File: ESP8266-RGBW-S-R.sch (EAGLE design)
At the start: 57 parts, among them IC1 ATTINY85, IC2 ESP8266-ESP12, IC6 LM1117-3.3, K1 SONGLE-RELAY-SPDT, K2 OMRON-G3MB-OPTO-RELAY, Q1 BC317, Q2 BC317, Q3 SO340020, Q4 SO340020, Q5 SO340020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

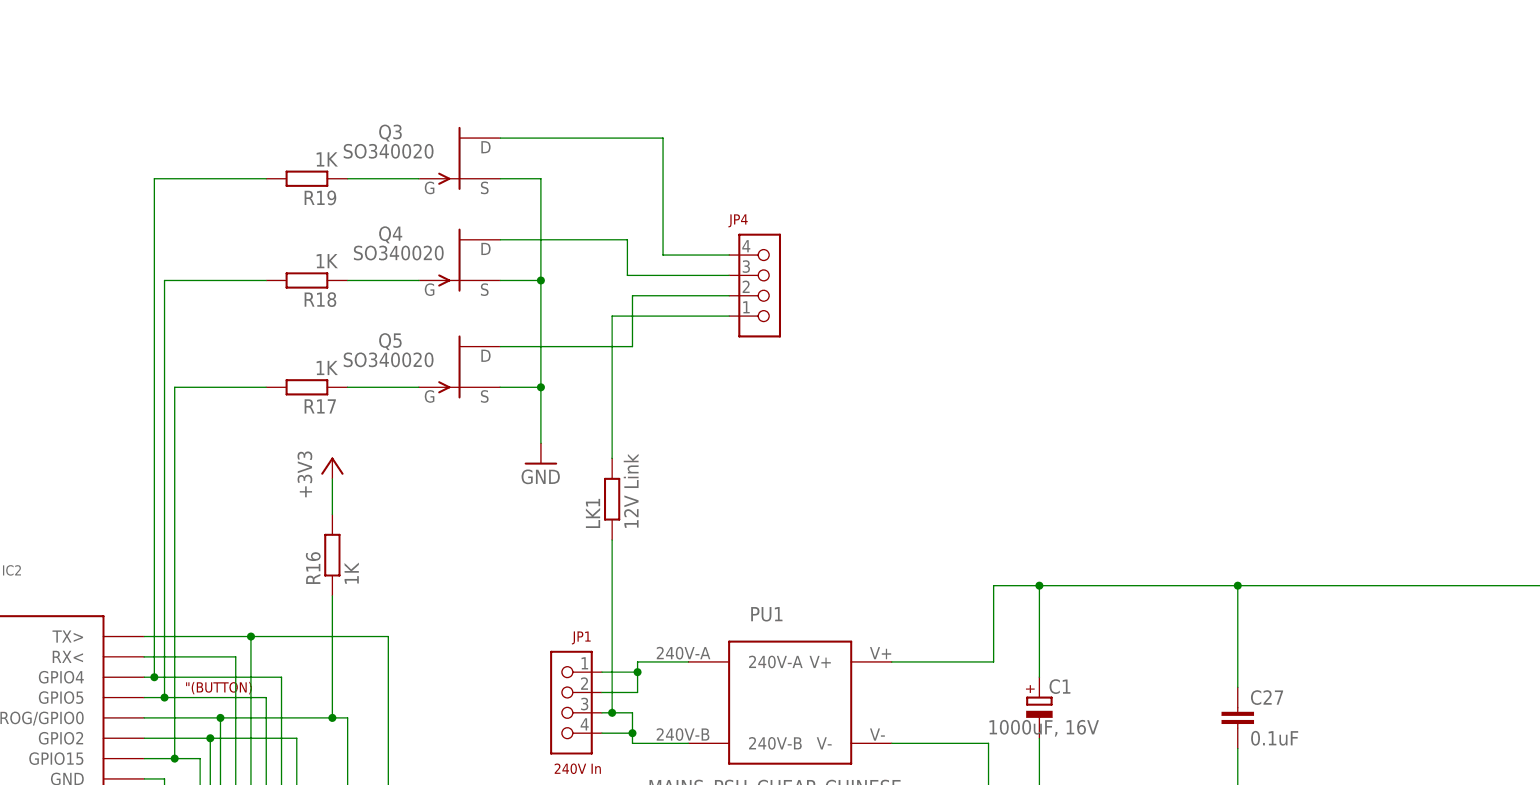
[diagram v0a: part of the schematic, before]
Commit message: added White channel for PWM output
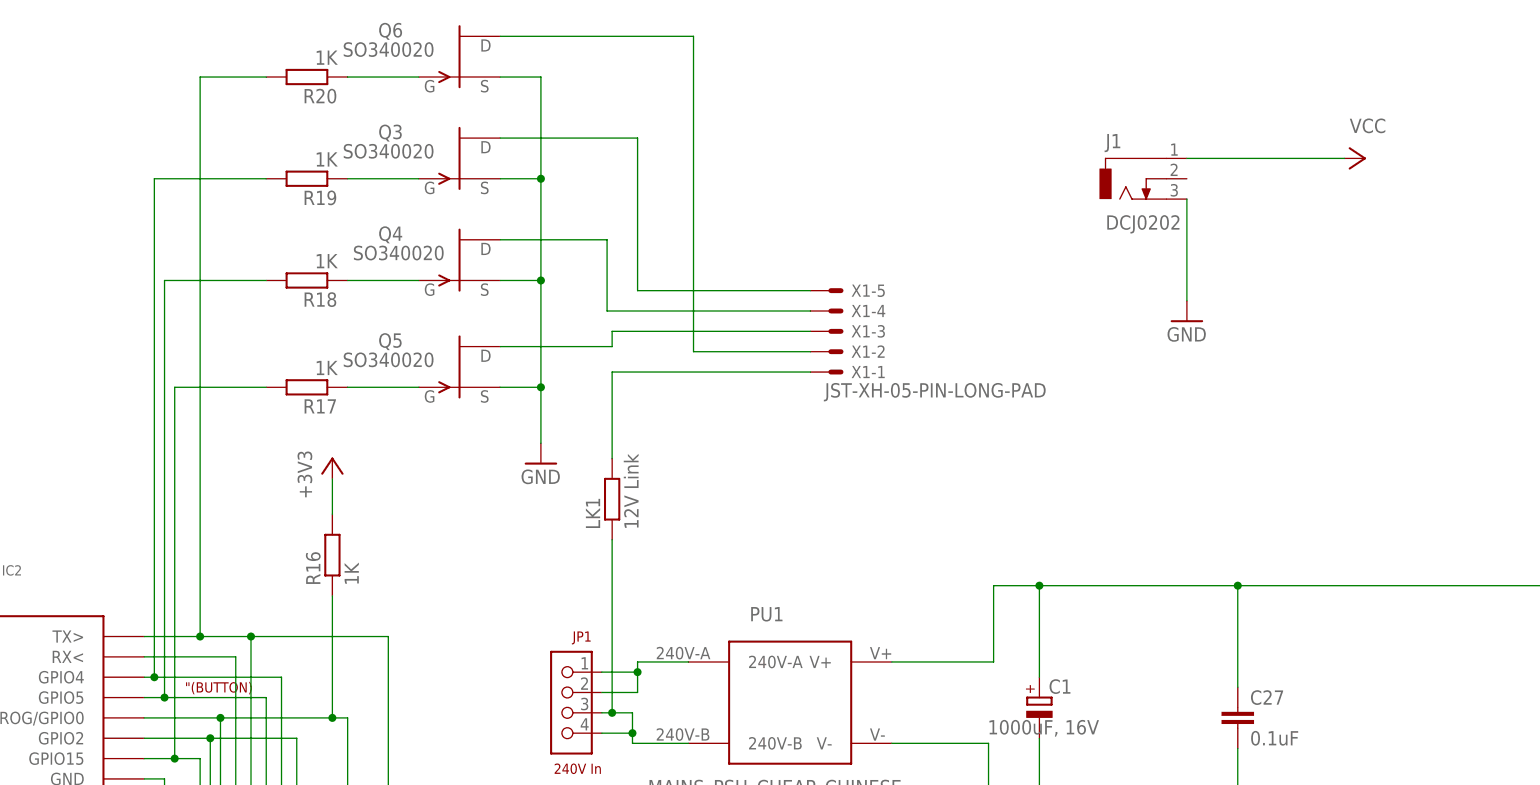
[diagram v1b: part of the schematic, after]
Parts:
- removed JP4: HDR4X0.1, Aidans:HDR4X0.1
- added J1: DCJ0202, con-jack:DCJ0202
- added Q6: SO340020, transistor-fet:SO340020
- added R20: 1K, resistor:R-EU_R0805
- added X1: JST-XH-05-PIN-LONG-PAD, Rembrandt Electronics - JST XH Connectors v1-0:JST-XH-05-PIN-LONG-PAD
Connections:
- removed net N$152: IC2.TX>, JP10.P$5, WIFI2.1
- new net GPIO3: IC2.TX>, JP10.P$5, R20.2, WIFI2.1
- new net N$117: Q3.D, X1-5.S
- new net N$118: Q6.G, R20.1
- net GND: now also J1.3, Q6.S
- net N$12: now also Q6.D, X1-2.S; no longer JP4.P$4, Q3.D
- net N$14: now also Q5.D, X1-3.S; no longer JP4.P$3, Q4.D
- net N$79: now also Q4.D, X1-4.S; no longer JP4.P$2, Q5.D
- net N$80: now also X1-1.S; no longer JP4.P$1
- net VCC: now also J1.1

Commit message: alternative power subbly (DC-DC, AC-DC), alternative power jack as input
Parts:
- removed PU1: MAINS_PSU_CHEAP_CHINESE, Aidans:MAINS_PSU_CHEAP_CHINESE
- added J3: WJ300-5.0, SparkFun-Connectors-2pin:CONN_02PTH4
- added JP4: V+V, pinhead:PINHD-1X2
- added PSU-A: HLK-PM013W, 5:HLK-PM013W
- added PSU-B: B0503S, dc-dc-converter:NME
- added PSU-C: DC-DC-STEP-DOWN-LM2596, diy-modules:DC-DC-STEP-DOWN-LM2596
- added PSU-D: HLK-2M03, HLK-2M03:HLK-2M03
- J1: value DCJ0202 -> POWER_JACKPTH_LOCK; device con-jack:DCJ0202 -> SparkFun-Connectors:POWER_JACKPTH_LOCK
- JP1: value 240V In -> GND+GND; device Aidans:4X0.2 -> pinhead:PINHD-1X2
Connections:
- removed net N$3: JP1.P$1, JP1.P$2, PU1.240V-A
- removed net N$5: JP1.P$3, JP1.P$4, LK1.1, PU1.240V-B
- new net +VCC: C1.+, C2.1, C27.1, C3.1, D1.C, IC6.IN, JP10.P$3, JP4.1, JP7.P$7, JP7.P$8, K1.C1, PSU-A.+VO
- new net V+: J1.PWR, J3.1, LK1.1, PSU-A.AC1, PSU-B.+VIN, PSU-C.IN+, PSU-D.AC_1
- new net V-: J1.GND, J3.2, PSU-A.AC2, PSU-B.-VIN, PSU-C.IN-, PSU-D.AC_2
- net +3V3: now also JP4.2
- net GND: now also JP1.1, JP1.2, PSU-A.-VO, PSU-B.-VOUT, PSU-C.OUT-, PSU-D.-VO; no longer J1.3, PU1.V-
- net GPIO2: now also JP5.P$3; no longer JP5.P$2
- net N$11: now also JP5.P$2
- net VCC: now also PSU-B.+VOUT, PSU-C.OUT+, PSU-D.+VO; no longer C1.+, C2.1, C27.1, C3.1, D1.C, IC6.IN, J1.1, JP10.P$3, JP7.P$7, JP7.P$8, K1.C1, PU1.V+
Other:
- moved on the sheet: C1, C2, C22, C27, C3, C4, IC6

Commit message: v 0.6
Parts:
- added R21: 4K7, resistor:R-EU_R0805
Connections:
- net +3V3: now also R21.2, R4.2, R5.1; no longer R4.1, R5.2
- net GPIO2: now also R4.1, R5.2; no longer R4.2, R5.1
- net N$11: now also R21.1
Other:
- moved on the sheet: R4, R5
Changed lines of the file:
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@@
 <part name="C4" library="resistor" deviceset="C-EU" device="C0805" value="0.1uF"/>
 <part name="JP5" library="Aidans" deviceset="HDR4X0.1" device="" value=""/>
-<part name="R5" library="resistor" deviceset="R-EU_" device="R0805" value="4K7"/>
+<part name="R4" library="resistor" deviceset="R-EU_" device="R0805" value="10K"/>
 <part name="K1" library="Aidans" deviceset="SONGLE-RELAY-SPDT" device=""/>
 <part name="JP8" library="Aidans" deviceset="3X0.2" device="" value="RELAY OUT"/>
@@
 <part name="R3" library="resistor" deviceset="R-EU_" device="R0805" value="10K"/>
 <part name="+3V12" library="supply1" deviceset="+3V3" device=""/>
-<part name="R4" library="resistor" deviceset="R-EU_" device="R0805" value="10K"/>
+<part name="R5" library="resistor" deviceset="R-EU_" device="R0805" value="4K7"/>
 <part name="SW1" library="Aidans" deviceset="VERTICAL-TACT-SWITCH" device=""/>
 <part name="GND11" library="supply1" deviceset="GND" device=""/>
@@
 <part name="SUPPLY4" library="supply2" deviceset="GND" device=""/>
 <part name="GND16" library="supply1" deviceset="GND" device=""/>
+<part name="R21" library="resistor" deviceset="R-EU_" device="R0805" value="4K7"/>
+<part name="+3V19" library="supply1" deviceset="+3V3" device=""/>
 </parts>
 <sheets>
@@
 <attribute name="VALUE" x="-81.915" y="-40.005" size="1.27" layer="94" rot="R180"/>
 </instance>
-<instance part="R5" gate="G$1" x="-42.545" y="-22.225" smashed="yes" rot="R90">
+<instance part="R4" gate="G$1" x="-42.545" y="-22.225" smashed="yes" rot="R90">
 <attribute name="NAME" x="-44.0436" y="-26.035" size="1.778" layer="95" rot="R90"/>
 <attribute name="VALUE" x="-39.243" y="-26.035" size="1.778" layer="96" rot="R90"/>
@@
 <attribute name="VALUE" x="125.73" y="40.64" size="1.778" layer="96" rot="R180"/>
 </instance>
-<instance part="R4" gate="G$1" x="34.925" y="64.135" smashed="yes" rot="R270">
+<instance part="R5" gate="G$1" x="34.925" y="64.135" smashed="yes" rot="R270">
 <attribute name="NAME" x="36.4236" y="67.945" size="1.778" layer="95" rot="R270"/>
 <attribute name="VALUE" x="31.623" y="67.945" size="1.778" layer="96" rot="R270"/>
@@
 <instance part="GND16" gate="1" x="310.515" y="133.35" smashed="yes">
 <attribute name="VALUE" x="307.975" y="130.81" size="1.778" layer="96"/>
+</instance>
+<instance part="R21" gate="G$1" x="-62.23" y="-22.225" smashed="yes" rot="R90">
+<attribute name="NAME" x="-63.7286" y="-26.035" size="1.778" layer="95" rot="R90"/>
+<attribute name="VALUE" x="-58.928" y="-26.035" size="1.778" layer="96" rot="R90"/>
+</instance>
+<instance part="+3V19" gate="G$1" x="-62.23" y="-10.795" smashed="yes">
+<attribute name="VALUE" x="-59.69" y="-8.255" size="1.778" layer="96" rot="R180"/>
 </instance>
 </instances>
@@
 </segment>
 <segment>
-<pinref part="R5" gate="G$1" pin="2"/>
+<pinref part="R4" gate="G$1" pin="2"/>
 <wire x1="-42.545" y1="-13.335" x2="-42.545" y2="-17.145" width="0.1524" layer="91"/>
 <pinref part="+3V3" gate="G$1" pin="+3V3"/>
@@
 </segment>
 <segment>
-<pinref part="R4" gate="G$1" pin="1"/>
+<pinref part="R5" gate="G$1" pin="1"/>
 <pinref part="+3V13" gate="G$1" pin="+3V3"/>
 <wire x1="34.925" y1="71.12" x2="34.925" y2="69.215" width="0.1524" layer="91"/>
@@
 <pinref part="+3V18" gate="G$1" pin="+3V3"/>
 <wire x1="18.415" y1="151.765" x2="18.415" y2="147.32" width="0.1524" layer="91"/>
+</segment>
+<segment>
+<pinref part="R21" gate="G$1" pin="2"/>
+<wire x1="-62.23" y1="-13.335" x2="-62.23" y2="-17.145" width="0.1524" layer="91"/>
+<pinref part="+3V19" gate="G$1" pin="+3V3"/>
 </segment>
 </net>
@@
 <wire x1="-69.215" y1="132.715" x2="-69.215" y2="102.235" width="0.1524" layer="91"/>
 <junction x="-69.215" y="102.235"/>
-<pinref part="R5" gate="G$1" pin="1"/>
+<pinref part="R4" gate="G$1" pin="1"/>
 <wire x1="-42.545" y1="-47.625" x2="-42.545" y2="-27.305" width="0.1524" layer="91"/>
 <wire x1="-42.545" y1="-47.625" x2="1.905" y2="-47.625" width="0.1524" layer="91"/>
 <pinref part="SW1" gate="G$1" pin="SW2"/>
-<pinref part="R4" gate="G$1" pin="2"/>
+<pinref part="R5" gate="G$1" pin="2"/>
 <wire x1="34.925" y1="59.055" x2="34.925" y2="57.15" width="0.1524" layer="91"/>
 <wire x1="34.925" y1="57.15" x2="34.925" y2="56.515" width="0.1524" layer="91"/>
@@
 <wire x1="-85.725" y1="120.015" x2="-116.84" y2="120.015" width="0.1524" layer="91"/>
 <pinref part="JP5" gate="G$1" pin="P$2"/>
-<wire x1="-80.645" y1="-47.625" x2="-47.625" y2="-47.625" width="0.1524" layer="91"/>
+<wire x1="-80.645" y1="-47.625" x2="-62.23" y2="-47.625" width="0.1524" layer="91"/>
+<wire x1="-62.23" y1="-47.625" x2="-47.625" y2="-47.625" width="0.1524" layer="91"/>
 <wire x1="-47.625" y1="-47.625" x2="-47.625" y2="119.38" width="0.1524" layer="91"/>
 <junction x="-47.625" y="119.38"/>
-</segment>
-</net>
+<pinref part="R21" gate="G$1" pin="1"/>
+<wire x1="-62.23" y1="-27.305" x2="-62.23" y2="-47.625" width="0.1524" layer="91"/>
+<junction x="-62.23" y="-47.625"/>
+</segment>
+</net>

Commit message: pull down resistors for the PWM control, some silkprint correction
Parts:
- added R22, R23, R24, R25: 10K, resistor:R-EU_R0805
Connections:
- net GND: now also R22.2, R23.2, R24.2, R25.2
- net N$112: now also R23.1
- net N$113: now also R24.1
- net N$118: now also R25.1
- net N$82: now also R22.1
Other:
- note added: "IRLML0040TRPBF"
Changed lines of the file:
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@@
 <part name="R21" library="resistor" deviceset="R-EU_" device="R0805" value="4K7"/>
 <part name="+3V19" library="supply1" deviceset="+3V3" device=""/>
+<part name="GND17" library="supply1" deviceset="GND" device=""/>
+<part name="R22" library="resistor" deviceset="R-EU_" device="R0805" value="10K"/>
+<part name="GND18" library="supply1" deviceset="GND" device=""/>
+<part name="R23" library="resistor" deviceset="R-EU_" device="R0805" value="10K"/>
+<part name="GND19" library="supply1" deviceset="GND" device=""/>
+<part name="R24" library="resistor" deviceset="R-EU_" device="R0805" value="10K"/>
+<part name="GND20" library="supply1" deviceset="GND" device=""/>
+<part name="R25" library="resistor" deviceset="R-EU_" device="R0805" value="10K"/>
 </parts>
 <sheets>
@@
 <text x="137.16" y="-46.355" size="1.778" layer="97">(c) 2015 Aidan Ruff &amp; Peter Scargill</text>
 <text x="137.16" y="-53.34" size="1.778" layer="97">(aidan@ruffs.org - pete@scargill.net)</text>
+<text x="31.75" y="215.265" size="1.778" layer="91">IRLML0040TRPBF</text>
 </plain>
 <instances>
@@
 <instance part="+3V19" gate="G$1" x="-62.23" y="-10.795" smashed="yes">
 <attribute name="VALUE" x="-59.69" y="-8.255" size="1.778" layer="96" rot="R180"/>
+</instance>
+<instance part="GND17" gate="1" x="26.67" y="145.415" smashed="yes">
+<attribute name="VALUE" x="24.13" y="142.875" size="1.778" layer="96"/>
+</instance>
+<instance part="R22" gate="G$1" x="25.4" y="156.21" smashed="yes" rot="R270">
+<attribute name="NAME" x="26.8986" y="160.02" size="1.778" layer="95" rot="R270"/>
+<attribute name="VALUE" x="22.098" y="160.02" size="1.778" layer="96" rot="R270"/>
+</instance>
+<instance part="GND18" gate="1" x="-20.955" y="155.575" smashed="yes">
+<attribute name="VALUE" x="-23.495" y="153.035" size="1.778" layer="96"/>
+</instance>
+<instance part="R23" gate="G$1" x="-20.955" y="175.895" smashed="yes" rot="R270">
+<attribute name="NAME" x="-19.4564" y="179.705" size="1.778" layer="95" rot="R270"/>
+<attribute name="VALUE" x="-24.257" y="179.705" size="1.778" layer="96" rot="R270"/>
+</instance>
+<instance part="GND19" gate="1" x="-31.115" y="155.575" smashed="yes">
+<attribute name="VALUE" x="-33.655" y="153.035" size="1.778" layer="96"/>
+</instance>
+<instance part="R24" gate="G$1" x="-31.115" y="175.895" smashed="yes" rot="R270">
+<attribute name="NAME" x="-29.6164" y="179.705" size="1.778" layer="95" rot="R270"/>
+<attribute name="VALUE" x="-34.417" y="179.705" size="1.778" layer="96" rot="R270"/>
+</instance>
+<instance part="GND20" gate="1" x="-41.91" y="155.575" smashed="yes">
+<attribute name="VALUE" x="-44.45" y="153.035" size="1.778" layer="96"/>
+</instance>
+<instance part="R25" gate="G$1" x="-41.91" y="175.895" smashed="yes" rot="R270">
+<attribute name="NAME" x="-40.4114" y="179.705" size="1.778" layer="95" rot="R270"/>
+<attribute name="VALUE" x="-45.212" y="179.705" size="1.778" layer="96" rot="R270"/>
 </instance>
 </instances>
@@
 <wire x1="310.7436" y1="144.2974" x2="310.7436" y2="135.89" width="0.1524" layer="91"/>
 <wire x1="310.7436" y1="135.89" x2="310.515" y2="135.89" width="0.1524" layer="91"/>
+</segment>
+<segment>
+<pinref part="R22" gate="G$1" pin="2"/>
+<pinref part="GND17" gate="1" pin="GND"/>
+<wire x1="25.4" y1="151.13" x2="26.67" y2="150.495" width="0.1524" layer="91"/>
+<wire x1="26.67" y1="150.495" x2="26.67" y2="147.955" width="0.1524" layer="91"/>
+</segment>
+<segment>
+<pinref part="R23" gate="G$1" pin="2"/>
+<pinref part="GND18" gate="1" pin="GND"/>
+<wire x1="-20.955" y1="170.815" x2="-20.955" y2="158.115" width="0.1524" layer="91"/>
+</segment>
+<segment>
+<pinref part="R24" gate="G$1" pin="2"/>
+<pinref part="GND19" gate="1" pin="GND"/>
+<wire x1="-31.115" y1="170.815" x2="-31.115" y2="158.115" width="0.1524" layer="91"/>
+</segment>
+<segment>
+<pinref part="R25" gate="G$1" pin="2"/>
+<pinref part="GND20" gate="1" pin="GND"/>
+<wire x1="-41.91" y1="170.815" x2="-41.91" y2="158.115" width="0.1524" layer="91"/>
 </segment>
 </net>
@@
 <pinref part="Q5" gate="G$1" pin="G"/>
 <pinref part="R17" gate="G$1" pin="1"/>
-<wire x1="20.32" y1="163.195" x2="29.21" y2="163.195" width="0.1524" layer="91"/>
+<wire x1="20.32" y1="163.195" x2="25.4" y2="163.195" width="0.1524" layer="91"/>
+<pinref part="R22" gate="G$1" pin="1"/>
+<wire x1="25.4" y1="163.195" x2="29.21" y2="163.195" width="0.1524" layer="91"/>
+<wire x1="25.4" y1="161.29" x2="25.4" y2="163.195" width="0.1524" layer="91"/>
+<junction x="25.4" y="163.195"/>
 </segment>
 </net>
@@
 <pinref part="Q4" gate="G$1" pin="G"/>
 <pinref part="R18" gate="G$1" pin="1"/>
-<wire x1="20.32" y1="176.53" x2="29.21" y2="176.53" width="0.1524" layer="91"/>
+<wire x1="20.32" y1="176.53" x2="22.225" y2="176.53" width="0.1524" layer="91"/>
+<pinref part="R23" gate="G$1" pin="1"/>
+<wire x1="22.225" y1="176.53" x2="29.21" y2="176.53" width="0.1524" layer="91"/>
+<wire x1="-20.955" y1="180.975" x2="-20.955" y2="203.835" width="0.1524" layer="91"/>
+<wire x1="-20.955" y1="203.835" x2="22.225" y2="203.835" width="0.1524" layer="91"/>
+<wire x1="22.225" y1="203.835" x2="22.225" y2="176.53" width="0.1524" layer="91"/>
+<junction x="22.225" y="176.53"/>
 </segment>
 </net>
@@
 <pinref part="Q3" gate="G$1" pin="G"/>
 <pinref part="R19" gate="G$1" pin="1"/>
-<wire x1="20.32" y1="189.23" x2="29.21" y2="189.23" width="0.1524" layer="91"/>
+<wire x1="20.32" y1="189.23" x2="25.4" y2="189.23" width="0.1524" layer="91"/>
+<pinref part="R24" gate="G$1" pin="1"/>
+<wire x1="25.4" y1="189.23" x2="29.21" y2="189.23" width="0.1524" layer="91"/>
+<wire x1="-31.115" y1="180.975" x2="-31.115" y2="207.645" width="0.1524" layer="91"/>
+<wire x1="-31.115" y1="207.645" x2="25.4" y2="207.645" width="0.1524" layer="91"/>
+<wire x1="25.4" y1="207.645" x2="25.4" y2="189.23" width="0.1524" layer="91"/>
+<junction x="25.4" y="189.23"/>
 </segment>
 </net>
@@
 <net name="N$118" class="0">
 <segment>
-<wire x1="20.32" y1="201.93" x2="29.21" y2="201.93" width="0.1524" layer="91"/>
+<wire x1="20.32" y1="201.93" x2="27.94" y2="201.93" width="0.1524" layer="91"/>
 <pinref part="R20" gate="G$1" pin="1"/>
 <pinref part="Q6" gate="G$1" pin="G"/>
-</segment>
-</net>
+<pinref part="R25" gate="G$1" pin="1"/>
+<wire x1="27.94" y1="201.93" x2="29.21" y2="201.93" width="0.1524" layer="91"/>
+<wire x1="-41.91" y1="180.975" x2="-41.91" y2="212.09" width="0.1524" layer="91"/>
+<wire x1="-41.91" y1="212.09" x2="27.94" y2="212.09" width="0.1524" layer="91"/>
+<wire x1="27.94" y1="212.09" x2="27.94" y2="201.93" width="0.1524" layer="91"/>
+<junction x="27.94" y="201.93"/>
+</segment>
+</net>
